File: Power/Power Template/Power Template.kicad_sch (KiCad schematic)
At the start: 2 parts

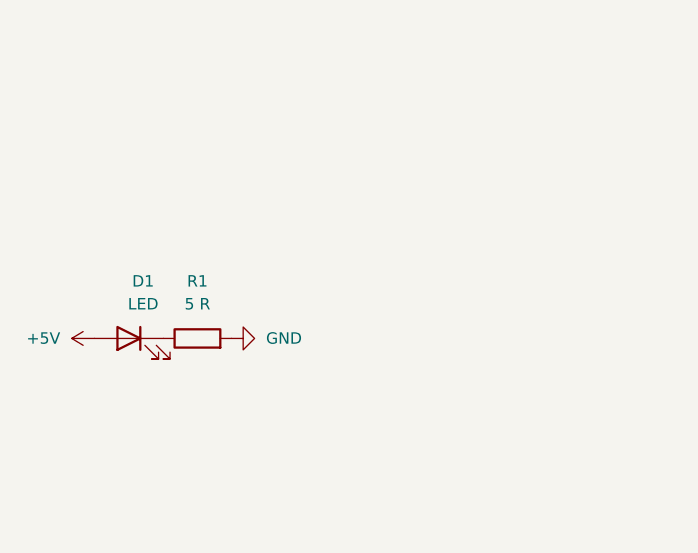
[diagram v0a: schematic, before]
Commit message: Added Arduino Uno to test file/folder
Just to show how fetching origin works
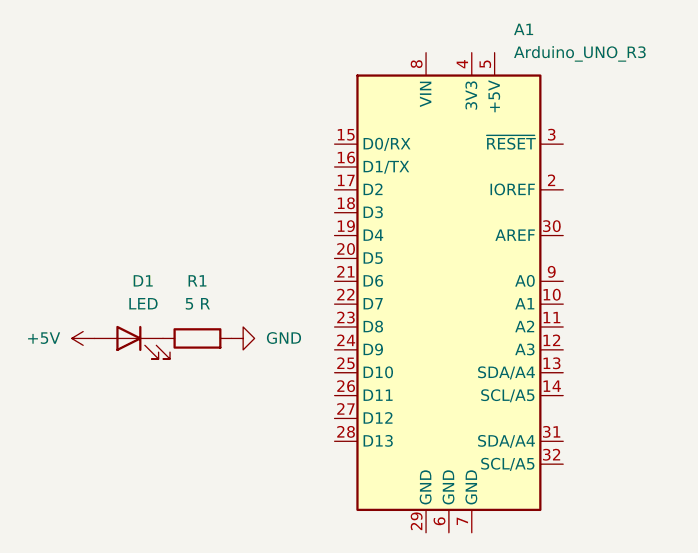
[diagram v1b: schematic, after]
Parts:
- added A1: Arduino_UNO_R3, Module:Arduino_UNO_R3, symbol MCU_Module:Arduino_UNO_R3
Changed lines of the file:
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@@
 	(paper "A4")
+	(symbol
+		(lib_id "MCU_Module:Arduino_UNO_R3")
+		(at 152.4 90.17 0)
+		(unit 1)
+		(exclude_from_sim no)
+		(in_bom yes)
+		(on_board yes)
+		(dnp no)
+		(fields_autoplaced yes)
+		(property "Reference" "A1"
+			(at 159.6233 62.23 0)
+			(effects
+				(font
+					(size 1.27 1.27)
+				)
+				(justify left)
+			)
+		)
+		(property "Value" "Arduino_UNO_R3"
+			(at 159.6233 64.77 0)
+			(effects
+				(font
+					(size 1.27 1.27)
+				)
+				(justify left)
+			)
+		)
+		(property "Footprint" "Module:Arduino_UNO_R3"
+			(at 152.4 90.17 0)
+			(effects
+				(font
+					(size 1.27 1.27)
+					(italic yes)
+				)
+				(hide yes)
+			)
+		)
+		(property "Datasheet" "https://www.arduino.cc/en/Main/arduinoBoardUno"
+			(at 152.4 90.17 0)
+			(effects
+				(font
+					(size 1.27 1.27)
+				)
+				(hide yes)
+			)
+		)
+		(property "Description" "Arduino UNO Microcontroller Module, release 3"
+			(at 152.4 90.17 0)
+			(effects
+				(font
+					(size 1.27 1.27)
+				)
+				(hide yes)
+			)
+		)
+		(pin "24"
+		)
+		(pin "26"
+		)
+		(pin "15"
+		)
+		(pin "19"
+		)
+		(pin "21"
+		)
+		(pin "25"
+		)
+		(pin "18"
+		)
+		(pin "14"
+		)
+		(pin "16"
+		)
+		(pin "29"
+		)
+		(pin "8"
+		)
+		(pin "17"
+		)
+		(pin "27"
+		)
+		(pin "6"
+		)
+		(pin "4"
+		)
+		(pin "23"
+		)
+		(pin "20"
+		)
+		(pin "28"
+		)
+		(pin "3"
+		)
+		(pin "30"
+		)
+		(pin "22"
+		)
+		(pin "7"
+		)
+		(pin "2"
+		)
+		(pin "1"
+		)
+		(pin "9"
+		)
+		(pin "10"
+		)
+		(pin "11"
+		)
+		(pin "12"
+		)
+		(pin "5"
+		)
+		(pin "13"
+		)
+		(pin "31"
+		)
+		(pin "32"
+		)
+		(instances
+			(project ""
+				(path "/25408cdd-ddcd-43a6-a2b3-38b538181112"
+					(reference "A1")
+					(unit 1)
+				)
+			)
+		)
+	)
 	(symbol
 		(lib_id "Device:R")

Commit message: Rev Neo added to repository
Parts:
- removed A1: Arduino_UNO_R3, Module:Arduino_UNO_R3, symbol MCU_Module:Arduino_UNO_R3
- removed D1: LED, symbol Device:LED
- removed R1: 5 R, symbol Device:R
